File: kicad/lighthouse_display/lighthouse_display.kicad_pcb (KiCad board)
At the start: 2 copper layers, 132 x 66.4 mm, 133 parts, among them J1 Conn_01x12_Pin, U1 IS31FL3731-SA, U2 TPS61176RTER

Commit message: hardware for lighthouse display rev1 and button rev1 done
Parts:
- added C9: 100nF, Capacitor_SMD:C_0603_1608Metric_Pad1.08x0.95mm_HandSolder, F.Cu at (53.3, 56.6)
- added U3: SHTC3, Sensor_Humidity:Sensirion_DFN-4-1EP_2x2mm_P1mm_EP0.7x1.6mm, F.Cu at (55.6, 56.2)
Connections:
- net /SCL renamed SCL
- net /SDA renamed SDA
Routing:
- net +3.3V: track 74.2 -> 153.0 mm, vias 2 -> 4
- net SDA: track 58.6 -> 128.5 mm, vias 4 -> 5
- net SCL: track 58.6 -> 127.9 mm, vias 4 -> 5
- net CB1: track 224.9 -> 221.9 mm
- net CB8: track 168.3 -> 165.6 mm
- net CB7: track 182.7 -> 180.1 mm
- net GND: track 35.1 -> 37.7 mm, vias 63 -> 72
- net CA2: vias 9 -> 8
- net (no net): vias 7 -> 0
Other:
- board text added: "Lighthouse display rev1 2024-10-26 MEgli"
- board text removed: "Lighthouse display rev 1 2024-10-10 MEgli"

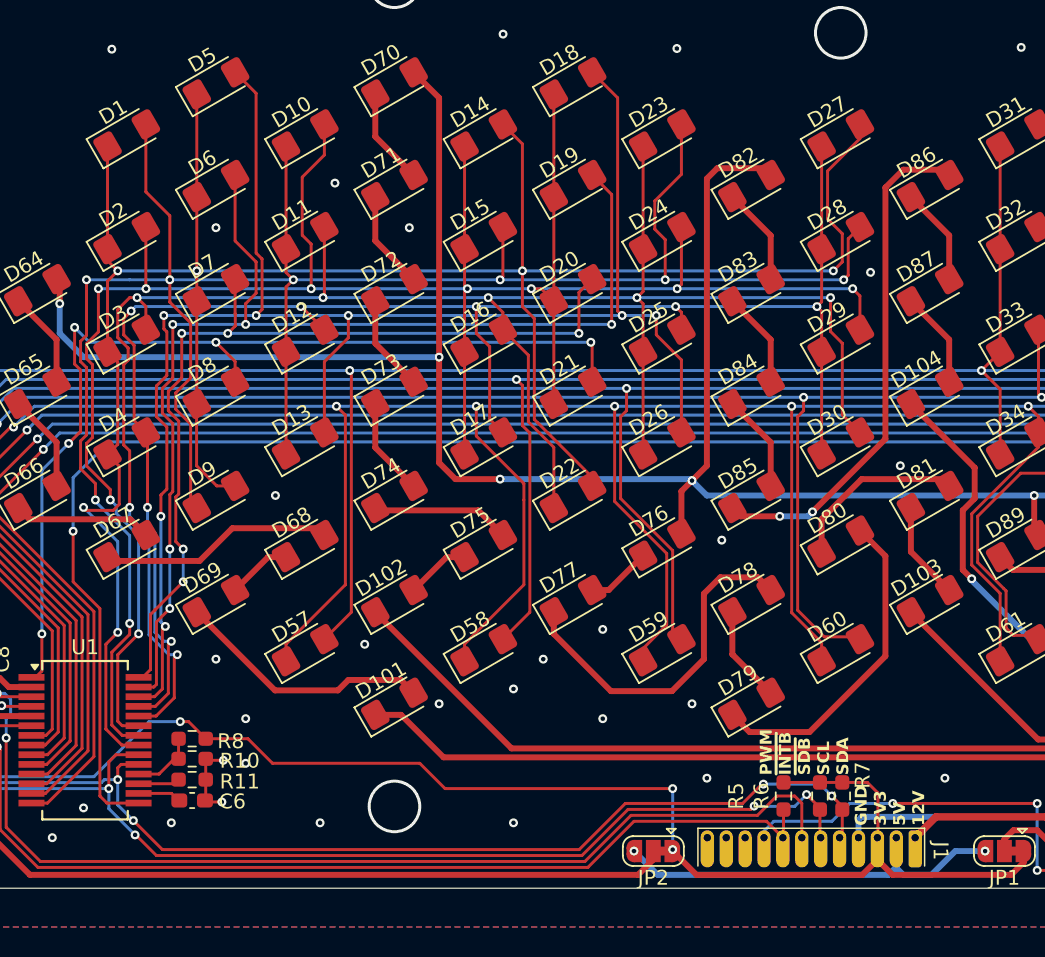
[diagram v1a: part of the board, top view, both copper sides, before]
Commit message: renamed libs + added opt3004 to lib
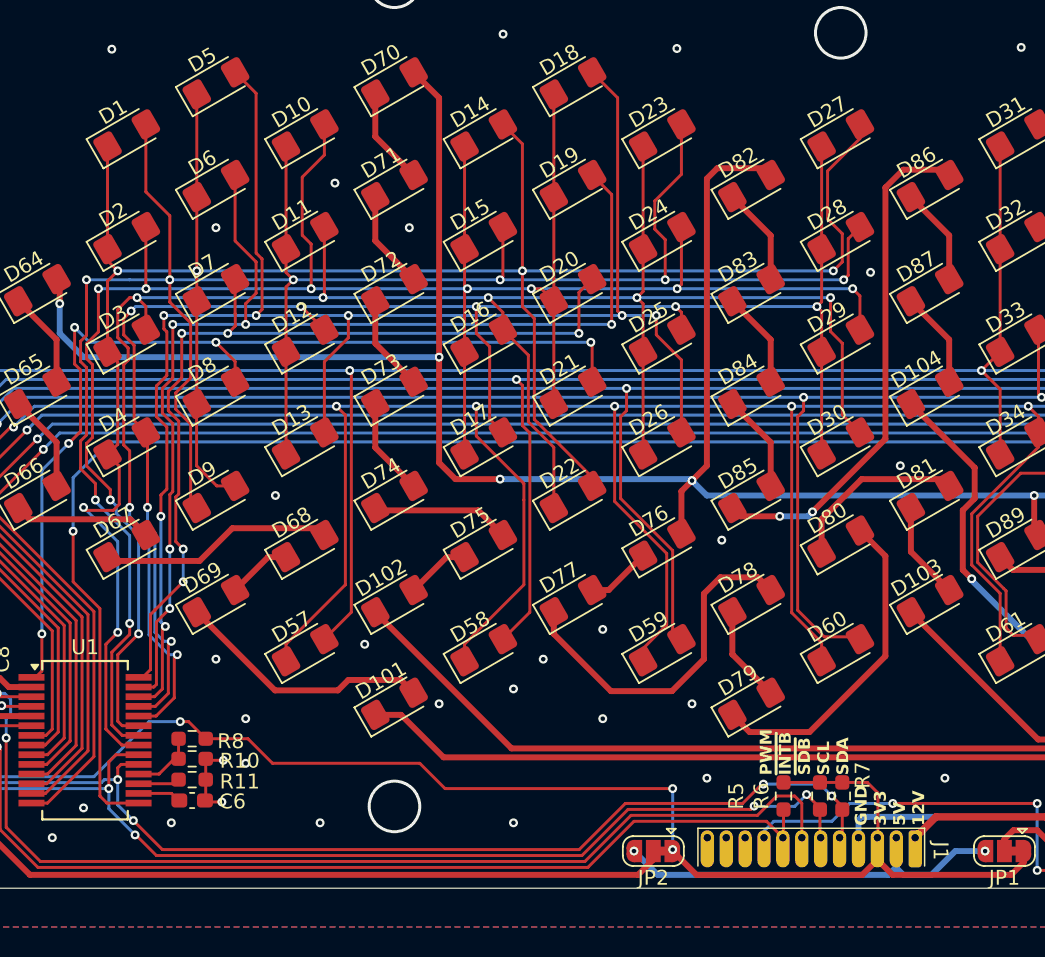
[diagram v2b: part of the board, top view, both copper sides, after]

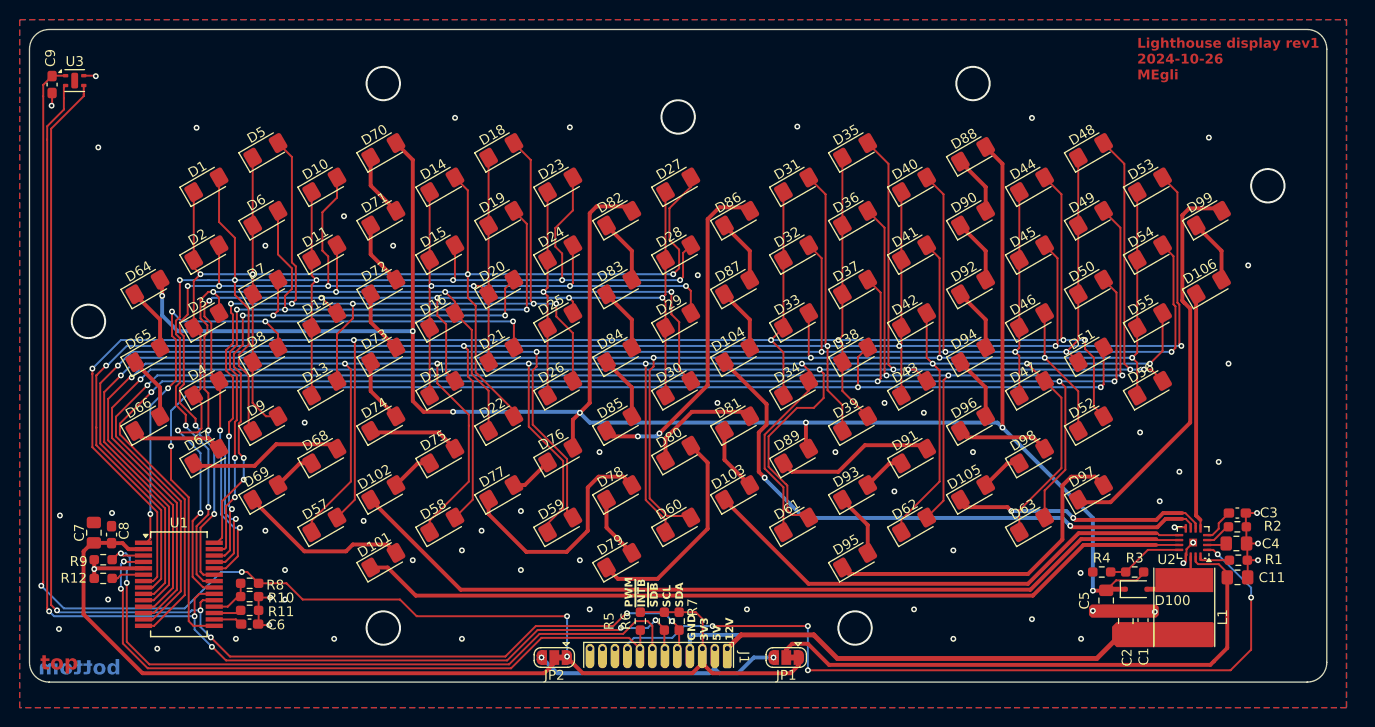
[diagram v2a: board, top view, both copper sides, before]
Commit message: ordererd lighthouse display
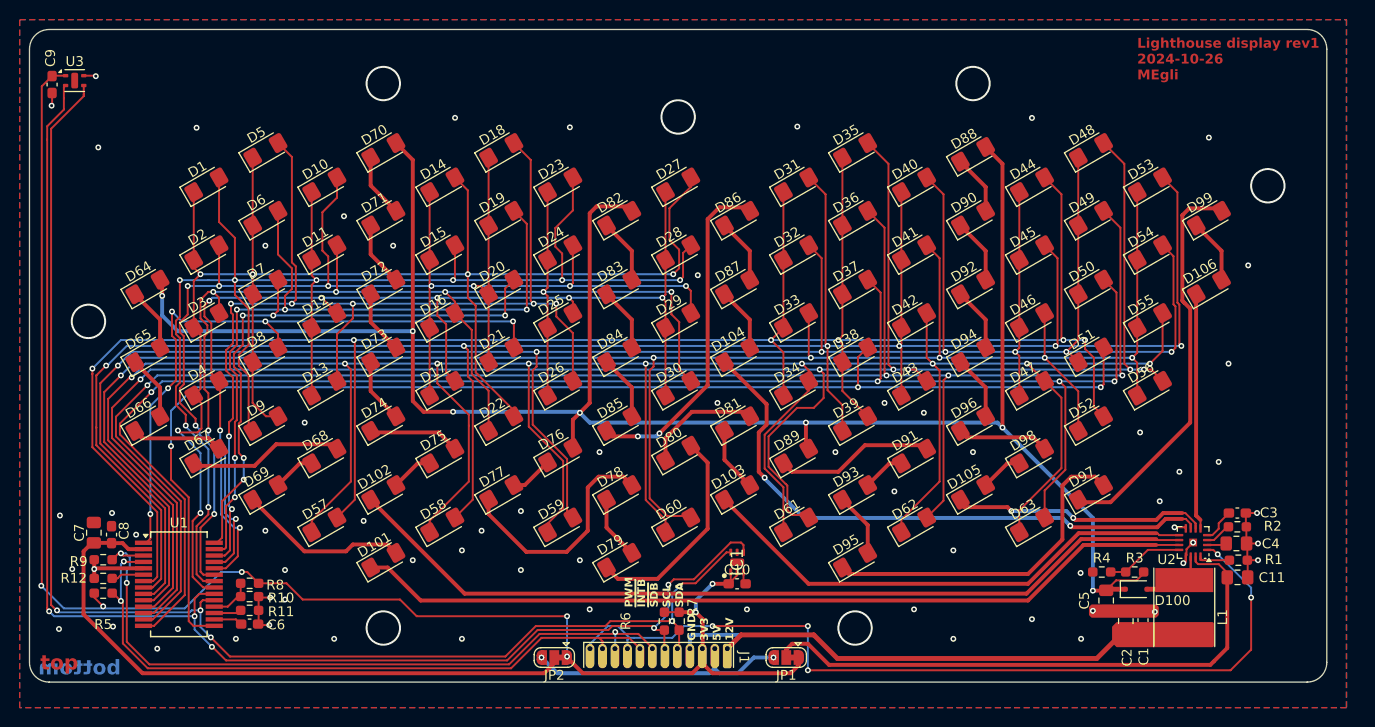
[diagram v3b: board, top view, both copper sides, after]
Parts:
- added C10: 100nF, Capacitor_SMD:C_0603_1608Metric_Pad1.08x0.95mm_HandSolder, F.Cu at (123.0, 107.4)
- added IC1: OPT3004DNPR, lighthouse:SON65P200X200X65-7N-D, F.Cu at (123.0, 105.2)
- D101, D102, D103, D104, D105, D106, D64, D65, D66, D67, D68, D69, D70, D71, D72, D73, D74, D75, D76, D77, D78, D79, D80, D81, D82, D83, D84, D85, D86, D87, D88, D89, D90, D91, D92, D93, D94, D95, D96, D97, D98, D99: value 1206MIL -> IN-S126AT5UW
- D12, D13, D16, D17, D21, D22, D25, D26, D29, D30, D33, D34, D38, D39, D42, D43, D46, D47, D51, D52, D57, D58, D59, D60, D61, D62, D63, D8, D9: value 1206MIL -> 599-0210-007F
- moved R5 54.7 mm to (58.5, 108.3), turned to 180 degrees
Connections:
- J1 pad 10: unconnected-(J1-Pin_10-Pad10) -> /~{SDB}
- J1 pad 11: unconnected-(J1-Pin_11-Pad11) -> /~{INTB}
- J1 pad 12: unconnected-(J1-Pin_12-Pad12) -> /WHITE_PWM
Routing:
- net SCL: track 127.9 -> 142.8 mm
- net SDA: track 128.5 -> 138.3 mm
- net +3.3V: track 153.0 -> 160.8 mm, vias 4 -> 7
- net /WHITE_PWM: track 82.8 -> 88.8 mm
- net GND: track 37.7 -> 39.0 mm, vias 72 -> 74
- net /~{INTB}: track 67.9 -> 68.5 mm
- net /~{SDB}: track 72.1 -> 71.6 mm, vias 2 -> 3
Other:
- board text added: "Front display User.9: all red LEDs"
- board text added: "back light User.7 white LEDs User.8 Back light, upper yellow, lower red"
